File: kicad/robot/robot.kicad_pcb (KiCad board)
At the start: 4 copper layers, 80 x 100 mm, 250 parts, among them IC1 TPS61253AYFFR, IC2 AP33771DKZ-13, IC3 EFC4626R-TR, J1 USBC_Receptacle_SMD_RA, J2 Conn_01x02, J3 67996-412HLF, J4 USB4120-03-C_REVA, Q1 Q_NMOS_GDS, Q2 EFC8811R-TF, U1 WRM483265-10F5-12V-G, U10 SN74AHC125RGYR, U11 MAX77958EWV+T, U12 BQ27742YZFR-G1, U13 MAX77976EFD+, U14 MAX77642ANA+, U15 ESD122DMYR, U2 W25Q128JVS, U3 RP2040, U4 NCP3901, U5 LSF0102DCTR, U6 MAX77857, U7 SN74AHC125RGYR, U8 DRV8830DRCR, U9 DRV8830DRCR, Y1 ABLS-12.000MHZ-B4-T

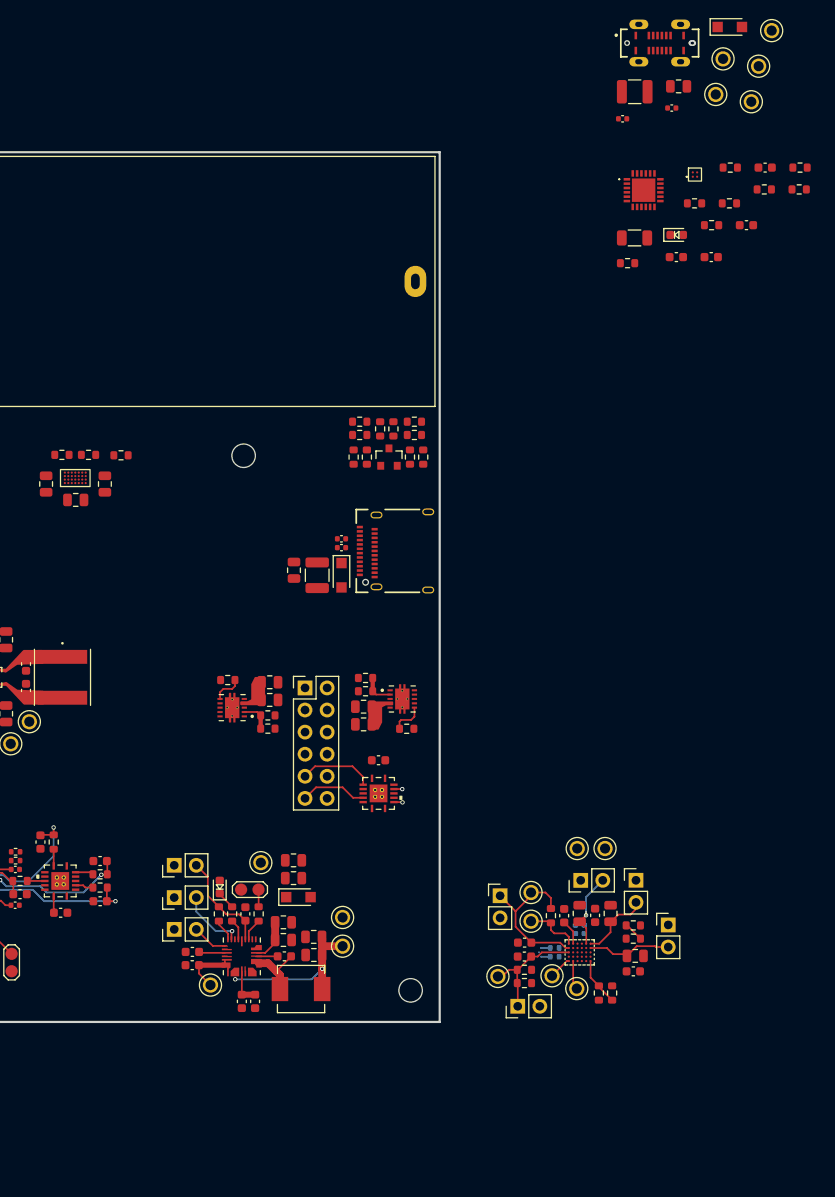
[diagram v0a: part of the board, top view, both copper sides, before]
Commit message: Moved bottom USB-C connector and parts to bottom
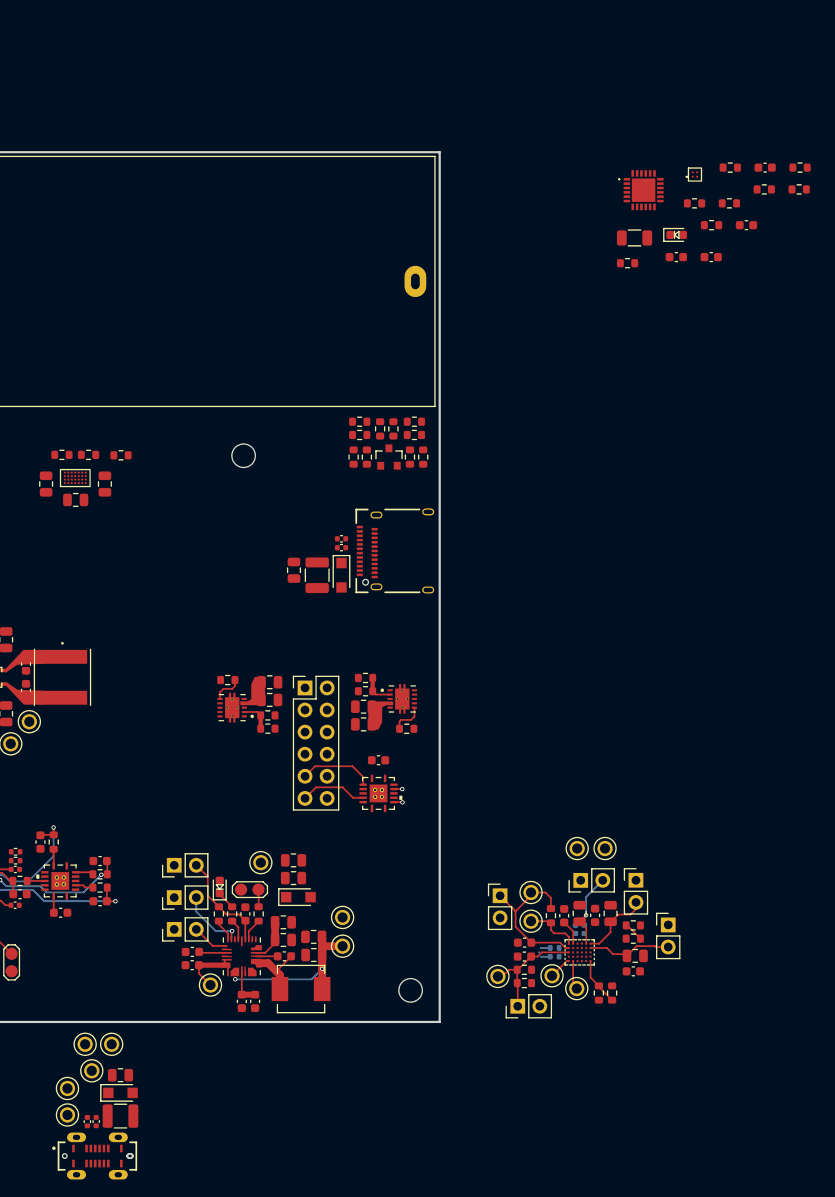
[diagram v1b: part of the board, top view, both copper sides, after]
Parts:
- moved TP15 148.7 mm to (97.2, 170.7)
- moved J4 143.4 mm to (100.6, 175.4)
- moved D3 141.2 mm to (103.3, 168.2)
- moved TP29 138.0 mm to (97.2, 167.6)
- moved TP30 137.1 mm to (100.0, 165.6)
- moved TP13 134.8 mm to (102.3, 162.6)
- moved C89 134.5 mm to (99.5, 171.5), turned to 90 degrees
- moved C96 131.8 mm to (103.3, 170.8)
- moved TP14 131.1 mm to (99.2, 162.6)
- moved C97 130.6 mm to (103.3, 166.1)
- moved C95 130.2 mm to (100.5, 171.5), turned to 90 degrees
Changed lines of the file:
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@@
   )
   (footprint "Capacitor_SMD:C_0402_1005Metric" (layer "F.Cu")
-    (at 161.03 56.16)
+    (at 100.505 171.459 90)
     (descr "Capacitor SMD 0402 (1005 Metric), square (rectangular) end terminal, IPC_7351 nominal, (Body size source: IPC-SM-782 page 76, https://www.pcb-3d.com/wordpress/wp-content/uploads/ipc-sm-782a_amendment_1_and_2.pdf), generated with kicad-footprint-generator")
     (tags "capacitor")
@@
     (property "Sheetname" "USB-C_PhonePC")
     (attr smd)
-    (fp_text reference "C95" (at 0 -1.16) (layer "F.SilkS") hide
+    (fp_text reference "C95" (at 0 -1.16 90) (layer "F.SilkS") hide
       (effects (font (size 1 1) (thickness 0.15)))
     )
-    (fp_text value "27pF" (at 0 1.16) (layer "F.Fab") hide
+    (fp_text value "27pF" (at 0 1.16 90) (layer "F.Fab") hide
       (effects (font (size 1 1) (thickness 0.15)))
     )
-    (fp_text user "${REFERENCE}" (at 0 0) (layer "F.Fab")
+    (fp_text user "${REFERENCE}" (at 0 0 90) (layer "F.Fab")
       (effects (font (size 0.25 0.25) (thickness 0.04)))
     )
@@
     (fp_line (start 0.5 0.25) (end -0.5 0.25) (layer "F.Fab") (width 0.1))
     (fp_line (start -0.5 0.25) (end -0.5 -0.25) (layer "F.Fab") (width 0.1))
-    (pad "1" smd roundrect (at -0.48 0) (size 0.56 0.62) (layers "F.Cu" "F.Paste" "F.Mask") (roundrect_rratio 0.25)
+    (pad "1" smd roundrect (at -0.48 0 90) (size 0.56 0.62) (layers "F.Cu" "F.Paste" "F.Mask") (roundrect_rratio 0.25)
       (net 32 "/USB-C_PhonePC/CC2") (pintype "passive"))
-    (pad "2" smd roundrect (at 0.48 0) (size 0.56 0.62) (layers "F.Cu" "F.Paste" "F.Mask") (roundrect_rratio 0.25)
+    (pad "2" smd roundrect (at 0.48 0 90) (size 0.56 0.62) (layers "F.Cu" "F.Paste" "F.Mask") (roundrect_rratio 0.25)
       (net 2 "GND") (pintype "passive"))
     (model "${KICAD6_3DMODEL_DIR}/Capacitor_SMD.3dshapes/C_0402_1005Metric.wrl"
@@
   )
   (footprint "Capacitor_SMD:C_0402_1005Metric" (layer "F.Cu")
-    (at 166.68 54.92)
+    (at 99.489 171.459 90)
     (descr "Capacitor SMD 0402 (1005 Metric), square (rectangular) end terminal, IPC_7351 nominal, (Body size source: IPC-SM-782 page 76, https://www.pcb-3d.com/wordpress/wp-content/uploads/ipc-sm-782a_amendment_1_and_2.pdf), generated with kicad-footprint-generator")
     (tags "capacitor")
@@
     (property "Sheetname" "USB-C_PhonePC")
     (attr smd)
-    (fp_text reference "C89" (at 0 -1.16) (layer "F.SilkS") hide
+    (fp_text reference "C89" (at 0 -1.16 90) (layer "F.SilkS") hide
       (effects (font (size 1 1) (thickness 0.15)))
     )
-    (fp_text value "27pF" (at 0 1.16) (layer "F.Fab") hide
+    (fp_text value "27pF" (at 0 1.16 90) (layer "F.Fab") hide
       (effects (font (size 1 1) (thickness 0.15)))
     )
-    (fp_text user "${REFERENCE}" (at 0 0) (layer "F.Fab")
+    (fp_text user "${REFERENCE}" (at 0 0 90) (layer "F.Fab")
       (effects (font (size 0.25 0.25) (thickness 0.04)))
     )
@@
     (fp_line (start 0.5 -0.25) (end 0.5 0.25) (layer "F.Fab") (width 0.1))
     (fp_line (start -0.5 -0.25) (end 0.5 -0.25) (layer "F.Fab") (width 0.1))
-    (pad "1" smd roundrect (at -0.48 0) (size 0.56 0.62) (layers "F.Cu" "F.Paste" "F.Mask") (roundrect_rratio 0.25)
+    (pad "1" smd roundrect (at -0.48 0 90) (size 0.56 0.62) (layers "F.Cu" "F.Paste" "F.Mask") (roundrect_rratio 0.25)
       (net 33 "/USB-C_PhonePC/CC1") (pintype "passive"))
-    (pad "2" smd roundrect (at 0.48 0) (size 0.56 0.62) (layers "F.Cu" "F.Paste" "F.Mask") (roundrect_rratio 0.25)
+    (pad "2" smd roundrect (at 0.48 0 90) (size 0.56 0.62) (layers "F.Cu" "F.Paste" "F.Mask") (roundrect_rratio 0.25)
       (net 2 "GND") (pintype "passive"))
     (model "${KICAD6_3DMODEL_DIR}/Capacitor_SMD.3dshapes/C_0402_1005Metric.wrl"
@@
   )
   (footprint "TestPoint:KEYSTONE_5002" (layer "F.Cu")
-    (at 178.17 46.02)
+    (at 97.203 170.697)
     (property "Sheetfile" "usb-c-phonepc.kicad_sch")
     (property "Sheetname" "USB-C_PhonePC")
@@
   )
   (footprint "TestPoint:KEYSTONE_5002" (layer "F.Cu")
-    (at 171.74 53.36)
+    (at 99.235 162.569)
     (property "Sheetfile" "usb-c-phonepc.kicad_sch")
     (property "Sheetname" "USB-C_PhonePC")
@@
   )
   (footprint "TestPoint:KEYSTONE_5002" (layer "F.Cu")
-    (at 175.83 54.2)
+    (at 97.203 167.649)
     (property "Sheetfile" "usb-c-phonepc.kicad_sch")
     (property "Sheetname" "USB-C_PhonePC")
@@
   )
   (footprint "Connector_USB:GCT_USB4120-03-C_REVA" (layer "F.Cu")
-    (at 165.295 47.45)
+    (at 100.644 175.419)
     (property "MANUFACTURER" "GCT")
     (property "MAXIMUM_PACKAGE_HEIGHT" "6.5mm")
@@
   )
   (footprint "Capacitor_SMD:C_0805_2012Metric" (layer "F.Cu")
-    (at 167.47 52.43)
+    (at 103.299 166.125)
     (descr "Capacitor SMD 0805 (2012 Metric), square (rectangular) end terminal, IPC_7351 nominal, (Body size source: IPC-SM-782 page 76, https://www.pcb-3d.com/wordpress/wp-content/uploads/ipc-sm-782a_amendment_1_and_2.pdf, https://docs.google.com/spreadsheets/d/1BsfQQcO9C6DZCsRaXUlFlo91Tg2WpOkGARC1WS5S8t0/edit?usp=sharing), generated with kicad-footprint-generator")
     (tags "capacitor")
@@
   )
   (footprint "Diode_SMD:Nexperia_CFP3_SOD-123W" (layer "F.Cu")
-    (at 173.355 45.6)
+    (at 103.299 168.157)
     (descr "Nexperia CFP3 (SOD-123W), https://assets.nexperia.com/documents/outline-drawing/SOD123W.pdf")
     (tags "CFP3 SOD-123W")
@@
       (effects (font (size 1 1) (thickness 0.15)))
     )
-    (fp_text user "${REFERENCE}" (at 0 -2) (layer "F.Fab")
+    (fp_text user "${REFERENCE}" (at -0.01158 0) (layer "F.Fab")
       (effects (font (size 1 1) (thickness 0.15)))
     )
@@
   )
   (footprint "TestPoint:KEYSTONE_5002" (layer "F.Cu")
-    (at 176.67 50.11)
+    (at 102.283 162.569)
     (property "Sheetfile" "usb-c-phonepc.kicad_sch")
     (property "Sheetname" "USB-C_PhonePC")
@@
   )
   (footprint "TestPoint:KEYSTONE_5002" (layer "F.Cu")
-    (at 172.58 49.27)
+    (at 99.997 165.617)
     (property "Sheetfile" "usb-c-phonepc.kicad_sch")
     (property "Sheetname" "USB-C_PhonePC")
@@
   )
   (footprint "Capacitor_SMD:C_1210_3225Metric" (layer "F.Cu")
-    (at 162.42 53.05)
+    (at 103.299 170.824)
     (descr "Capacitor SMD 1210 (3225 Metric), square (rectangular) end terminal, IPC_7351 nominal, (Body size source: IPC-SM-782 page 76, https://www.pcb-3d.com/wordpress/wp-content/uploads/ipc-sm-782a_amendment_1_and_2.pdf), generated with kicad-footprint-generator")
     (tags "capacitor")

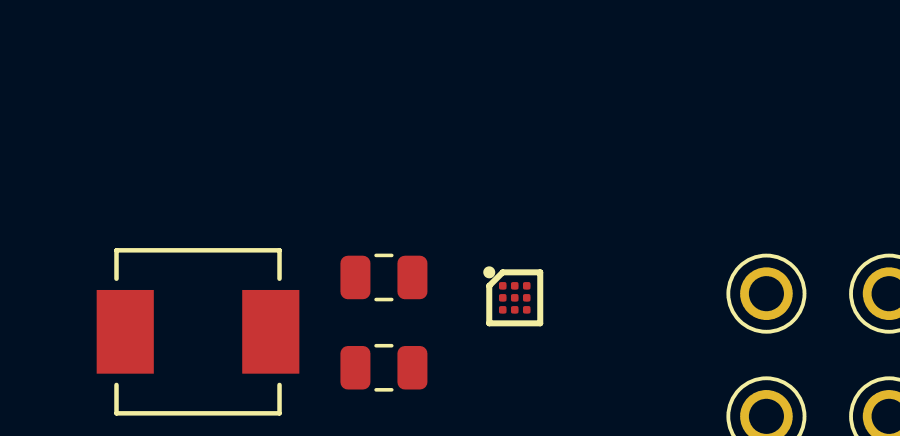
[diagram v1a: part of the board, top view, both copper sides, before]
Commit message: Added in dual mosfet and resistor to pcb
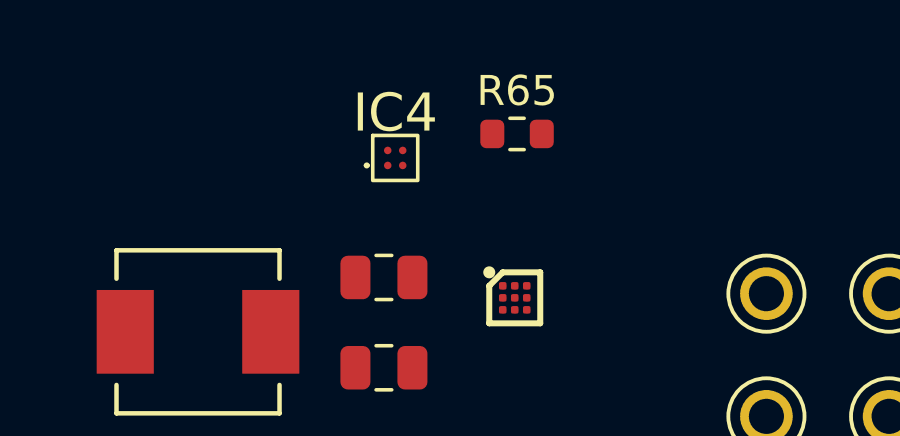
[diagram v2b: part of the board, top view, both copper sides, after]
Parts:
- added IC4: EFC4626R-TR, Package_BGA:ON_SEMI_EFCP1010-4DG-020, F.Cu at (197.2, 41.5)
- added R65: 100, Resistor_SMD:R_0603_1608Metric, F.Cu at (201.3, 40.7)
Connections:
- C100 pad 1: Net-(C100-Pad1) -> Net-(IC1-PadA1)
- C50 pad 1: Net-(C100-Pad1) -> Net-(C50-Pad1)
- C98 pad 1: Net-(C100-Pad1) -> Net-(IC1-PadA1)
- C99 pad 1: Net-(C100-Pad1) -> Net-(IC1-PadA1)
- IC1 pad A1: Net-(C100-Pad1) -> Net-(IC1-PadA1)
- IC1 pad A2: Net-(C100-Pad1) -> Net-(IC1-PadA1)
- JP4 pad 2: Net-(C100-Pad1) -> Net-(C50-Pad1)
- U11 pad A6: Net-(C100-Pad1) -> Net-(C50-Pad1)
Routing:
- net Net-(C50-Pad1): track 0.00 -> 8.31 mm
- net Net-(C100-Pad1): track 8.31 -> 0.00 mm

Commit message: continue to layut
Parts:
- C18, C19, C73, R26, R27, R29, R30: moved to B.Cu
- moved JP1 175.6 mm to (65.7, 147.1)
- moved TP1 164.9 mm to (34.3, 94.4)
- moved TP2 155.6 mm to (35.8, 91.6)
- moved R65 155.4 mm to (85.5, 144.3), turned to -90 degrees
- moved TP5 151.7 mm to (46.2, 80.6)
- moved TP4 150.5 mm to (44.7, 89.1)
- moved IC4 150.2 mm to (87.8, 144.3), turned to 180 degrees
- moved TP3 149.7 mm to (39.6, 80.4)
- moved TP6 149.6 mm to (44.4, 86.0)
- moved IC1 144.9 mm to (90.6, 139.7), turned to 90 degrees
- moved C98 141.4 mm to (87.1, 137.7), turned to 180 degrees
- moved C101 139.6 mm to (94.5, 140.4), turned to 180 degrees
- moved C100 139.0 mm to (87.1, 141.8), turned to 180 degrees
- moved L4 137.6 mm to (93.0, 144.2), turned to 180 degrees
- moved C99 134.3 mm to (87.1, 139.7), turned to 180 degrees
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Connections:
- J3 pad 2: /MOTORS/OUT_P2 -> /MOTORS/OUT_N2
- J3 pad 4: /MOTORS/OUT_N2 -> /MOTORS/OUT_P2
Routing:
- net /USB-C_PhonePC/VBUS: track 0.00 -> 27.7 mm
- net /SCL_SL: track 0.00 -> 17.0 mm, vias 0 -> 1
- net /GPIO16: track 0.00 -> 16.2 mm, vias 0 -> 4
- net /SYS: track 27.7 -> 43.8 mm
- net /USB-C_ExtChg/VBUS: track 0.00 -> 15.6 mm, vias 0 -> 2
- net /SDA_SL: track 0.00 -> 14.8 mm, vias 0 -> 1
- net /MOTORS/ENC_21: track 1.00 -> 15.6 mm
- net /USB-C_ExtChg/D-: track 0.00 -> 12.5 mm, vias 0 -> 2
- net /USB-C_PhonePC/D-: track 1.04 -> 13.4 mm, vias 0 -> 2
- net /USB-C_ExtChg/CC1: track 0.00 -> 12.0 mm, vias 0 -> 1
- net /USB-C_PhonePC/CC2: track 0.00 -> 11.1 mm, vias 0 -> 3
- net /USB-C_ExtChg/CC2: track 0.00 -> 11.0 mm, vias 0 -> 1
- net /PowerMux/FLAG: track 0.00 -> 9.89 mm, vias 0 -> 2
- net /USB-C_PhonePC/D+: track 1.04 -> 10.8 mm
- net /USB-PD-PhonePC/GPIO3: track 0.00 -> 9.72 mm, vias 0 -> 3
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- added copper zone on F.Cu, net /5V
- added copper zone on F.Cu, net /Charger/BATT
- added copper zone on F.Cu, net /Charger/V_IN
- added copper zone on F.Cu, net /MOTORS/OUT_N1
- added copper zone on F.Cu, net /MOTORS/OUT_N2
- added copper zone on F.Cu, net /MOTORS/OUT_P1
- added copper zone on F.Cu, net /MOTORS/OUT_P2
- added copper zone on F.Cu, net /PowerMux/VIN_A
- added copper zone on F.Cu, net /PowerMux/VIN_B
- added copper zone on F.Cu, net /SYS
- added copper zone on F.Cu, net /USB-C_ExtChg/VBUS
- added copper zone on F.Cu, net /VBoost
- added copper zone on F.Cu, net Net-(C100-Pad1)
- added copper zone on F.Cu, net Net-(C30-Pad2)
- added copper zone on F.Cu, net Net-(C31-Pad1)
- added copper zone on F.Cu, net Net-(C62-Pad1)
- added copper zone on F.Cu, net Net-(C73-Pad2)
- added copper zone on F.Cu, net Net-(C77-Pad1)
- added copper zone on F.Cu, net Net-(IC1-PadB1)

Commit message: continue to layout
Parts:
- removed IC3, IC4: EFC4626R-TR, Package_BGA:ON_SEMI_EFCP1010-4DG-020
- added Q3: YJL3416A, Package_TO_SOT_SMD:SOT-23, F.Cu at (118.0, 85.5)
- added Q4: YJL3416A, Package_TO_SOT_SMD:SOT-23, F.Cu at (114.1, 88.2)
- added R66: DNP, Resistor_SMD:R_0603_1608Metric, F.Cu at (114.5, 85.7)
- added U16: fpf1048bucx, Package_BGA:BGA6N50P3X2_146X96X62N, F.Cu at (89.1, 145.8)
- C11, C14, C15, C17, C2, C3, C37, C7, D3, R23, R5: moved to B.Cu
- R65: value 100 -> 10M
- moved H3 86.6 mm to (137.0, 108.0)
- moved R31 81.9 mm to (124.1, 157.7), turned to -90 degrees
- moved U9 81.9 mm to (126.9, 157.1), turned to -90 degrees
- moved R27 78.5 mm to (128.2, 154.4), turned to 0 degrees
- moved C44 78.3 mm to (119.0, 155.7), turned to 90 degrees
- moved U10 78.2 mm to (115.8, 155.8), turned to -90 degrees
- moved H4 76.5 mm to (63.0, 86.0)
- moved R30 76.4 mm to (128.2, 152.9), turned to 0 degrees
- moved C41 76.3 mm to (125.6, 153.4), turned to 90 degrees
- moved C43 75.8 mm to (123.5, 153.4), turned to 90 degrees
- moved J3 68.7 mm to (128.0, 147.3), turned to -90 degrees
- moved C42 64.5 mm to (131.4, 143.1), turned to -90 degrees
- moved R26 64.0 mm to (126.7, 144.2), turned to 180 degrees
- moved C40 63.6 mm to (129.3, 143.1), turned to -90 degrees
- moved R29 61.9 mm to (126.7, 142.7), turned to 180 degrees
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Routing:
- net /USB-C_PhonePC/VBUS: track 27.7 -> 13.7 mm, vias 0 -> 3
- net /SYS: track 43.8 -> 30.2 mm
- net /USB-PD-PhonePC/VIO1_: track 18.1 -> 4.57 mm
- net /MCU/XIN: track 14.0 -> 4.16 mm, vias 0 -> 1
- net /MCU/GPIO28_ADC2: track 16.2 -> 7.42 mm, vias 2 -> 1
- net /MCU/RUN: track 8.79 -> 0.39 mm
- net /MCU/SWD: track 6.72 -> 0.00 mm
- net /3V3: track 26.1 -> 22.1 mm, vias 0 -> 2
- net /USB-PD-PhonePC/VIO1: track 0.00 -> 3.68 mm
- net Net-(Q3-Pad1): track 3.61 -> 0.17 mm
- net /SCL_SL: track 17.0 -> 14.1 mm
- net Net-(R65-Pad1): track 2.86 -> 0.00 mm
- net /USB-C_PhonePC/CC1: track 7.68 -> 4.84 mm
- net Net-(IC2-Pad24): track 2.48 -> 0.02 mm
- net Net-(C100-Pad1): track 2.35 -> 0.00 mm
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- added copper zone on B.Cu, net /USB-C_PhonePC/VBUS
- added copper zone on F.Cu, net /USB-C_PhonePC/VBUS
- removed copper zone on F.Cu, net Net-(C100-Pad1)
- removed copper zone on F.Cu, net Net-(IC1-PadB1)
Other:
- board size 80 x 100 mm -> 80 x 77 mm
